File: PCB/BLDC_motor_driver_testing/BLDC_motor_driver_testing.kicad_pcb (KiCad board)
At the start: 4 copper layers, 90 x 63 mm, 84 parts, among them J1 PWR, J2 PHASE A, J3 PHASE B, J4 PHASE C, Q1 IRF540N, Q2 IRF540N, Q3 IRF540N, Q4 IRF540N, Q5 IRF540N, Q6 IRF540N, U1 AMS1117-3.3, U10 LMV393, U2 IR2104, U3 INA240A2D, U4 LMV393, U5 IR2104, U6 INA240A2D, U7 LMV393, U8 IR2104, U9 INA240A2D

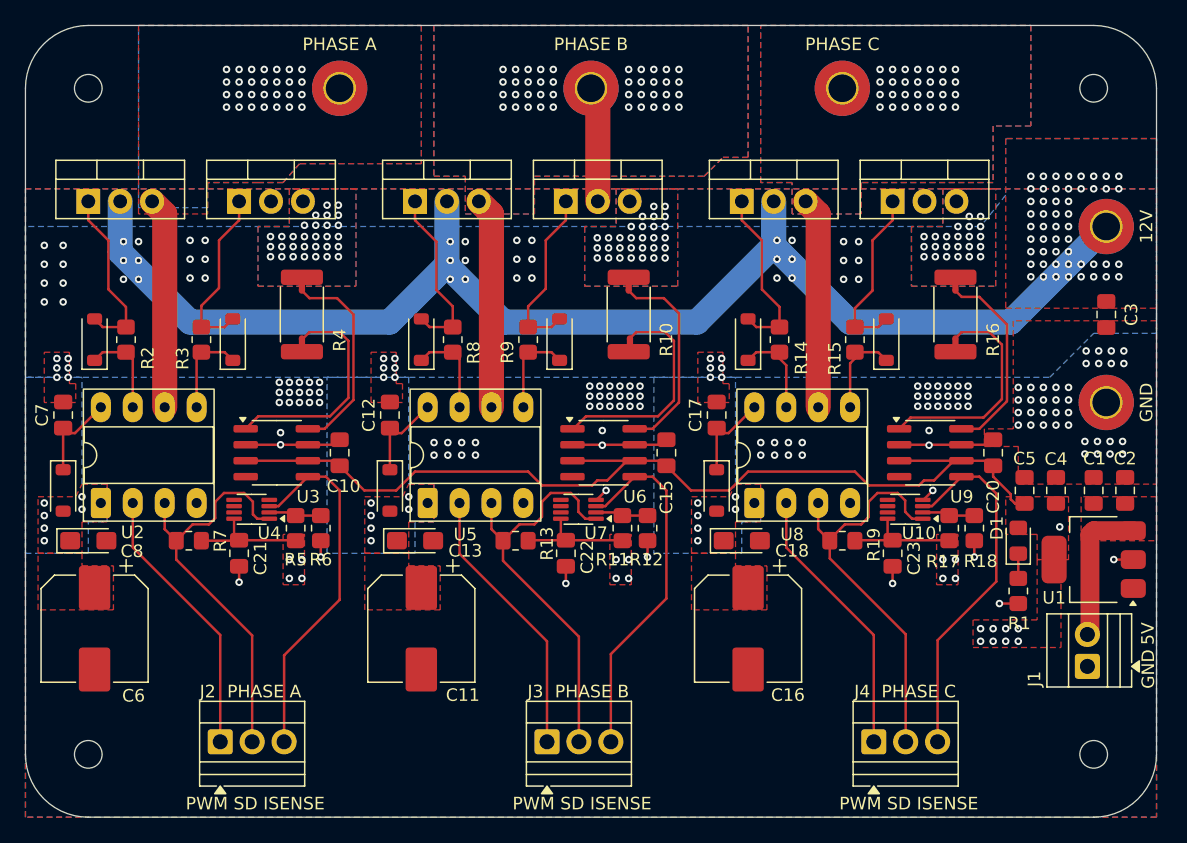
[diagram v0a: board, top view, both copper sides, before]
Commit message: Final version of BLDC test driver
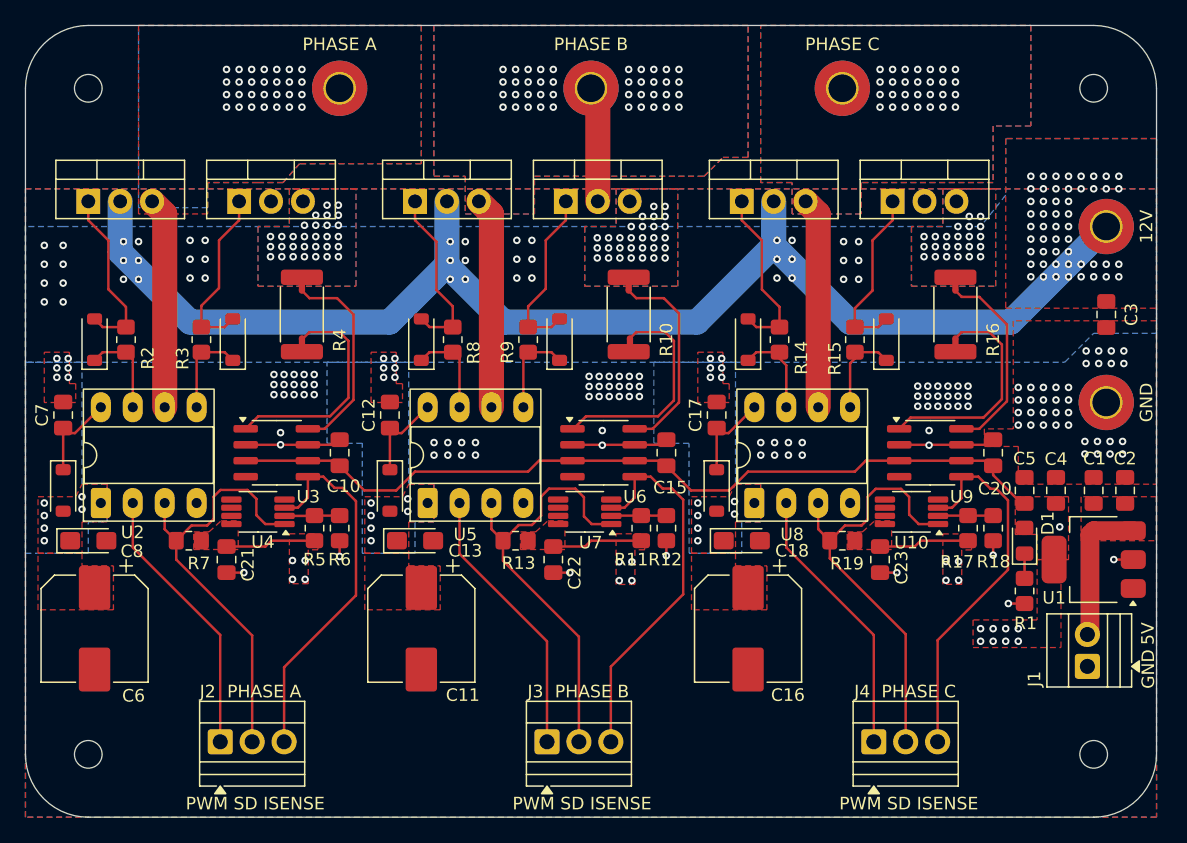
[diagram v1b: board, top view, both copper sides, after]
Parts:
- C11, C16, C6: value 470u -> 220u
- U10, U4, U7: footprint Package_SO:VSSOP-8_2.3x2mm_P0.5mm -> Package_SO:VSSOP-8_3x3mm_P0.65mm
- moved R11 1.50 mm to (69.0, 60.0)
- moved R12 1.50 mm to (71.0, 60.0)
- moved R17 1.50 mm to (95.0, 60.0)
- moved R18 1.50 mm to (97.0, 60.0)
- moved R5 1.50 mm to (43.0, 60.0)
- moved R6 1.50 mm to (45.0, 60.0)
- moved C21 1.12 mm to (36.0, 62.5)
- moved C22 1.12 mm to (62.0, 62.5)
- moved C23 1.12 mm to (88.0, 62.5)
- moved U10 0.54 mm to (90.5, 58.7)
- moved U4 0.54 mm to (38.5, 58.7)
- moved U7 0.54 mm to (64.5, 58.7)
- moved D1 0.50 mm to (99.5, 61.0)
- moved R1 0.50 mm to (99.5, 65.0)
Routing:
- net +3.3V: track 115.2 -> 98.6 mm
- net GND: track 34.9 -> 32.2 mm, vias 118 -> 116
- net SD_C: track 33.0 -> 35.3 mm
- net SD_B: track 32.9 -> 35.2 mm
- net SD_A: track 33.1 -> 35.1 mm
- net ISENSE_B: track 28.9 -> 30.1 mm
- net ISENSE_A: track 28.9 -> 30.0 mm
- net ISENSE_C: track 29.1 -> 29.9 mm
